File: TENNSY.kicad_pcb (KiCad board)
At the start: 2 copper layers, 120 x 160 mm, 27 parts, among them J1 HEADER_2, J2 HEADER_2, U1 Teensy4.0, U2 DRV8872, U3 QRE1113, U4 QRE1113, U5 QRE1113, U6 QRE1113, U7 QRE1113, U8 DRV8872

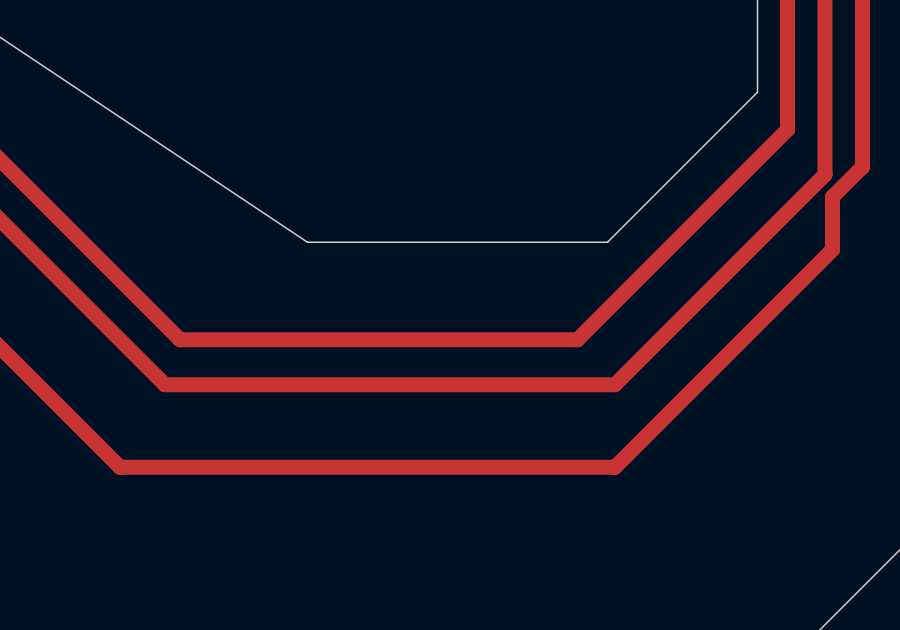
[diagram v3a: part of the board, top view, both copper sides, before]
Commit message: modificaciones
se modifico sch,pcb:
se agrego una llave
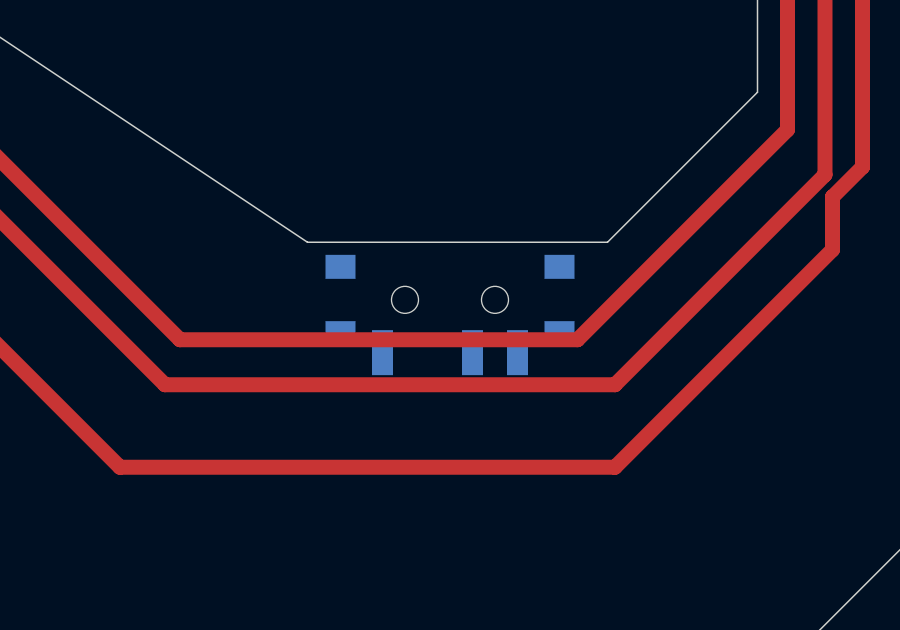
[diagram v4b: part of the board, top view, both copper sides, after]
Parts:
- added REF**: SW_SPDT_PCM12, Button_Switch_SMD:SW_SPDT_PCM12, B.Cu at (134.8, 137.2)
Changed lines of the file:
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@@
     (tracks 125)
     (zones 0)
-    (modules 27)
+    (modules 28)
     (nets 20)
   )
@@
     (add_net "Net-(R9-Pad2)")
   )
+  (module Button_Switch_SMD:SW_SPDT_PCM12 (layer B.Cu)
+    (at 134.75 137.25)
+    (descr "Ultraminiature Surface Mount Slide Switch, right-angle, https://www.ckswitches.com/media/1424/pcm.pdf")
+    (attr smd)
+    (fp_text reference REF** (at 0 3.2) (layer B.SilkS)
+      (effects (font (size 1 1) (thickness 0.15)) (justify mirror))
+    )
+    (fp_text value SW_SPDT_PCM12 (at 0 -4.25) (layer B.Fab)
+      (effects (font (size 1 1) (thickness 0.15)) (justify mirror))
+    )
+    (fp_line (start 3.45 -0.72) (end 3.45 0.07) (layer B.SilkS) (width 0.12))
+    (fp_line (start -3.45 0.07) (end -3.45 -0.72) (layer B.SilkS) (width 0.12))
+    (fp_line (start -1.6 1.12) (end 0.1 1.12) (layer B.SilkS) (width 0.12))
+    (fp_line (start -2.85 -1.73) (end 2.85 -1.73) (layer B.SilkS) (width 0.12))
+    (fp_line (start -0.1 -3.02) (end -0.1 -1.73) (layer B.SilkS) (width 0.12))
+    (fp_line (start -1.2 -3.23) (end -0.3 -3.23) (layer B.SilkS) (width 0.12))
+    (fp_line (start -1.4 -1.73) (end -1.4 -3.02) (layer B.SilkS) (width 0.12))
+    (fp_line (start -0.1 -3.02) (end -0.3 -3.23) (layer B.SilkS) (width 0.12))
+    (fp_line (start -1.4 -3.02) (end -1.2 -3.23) (layer B.SilkS) (width 0.12))
+    (fp_line (start -4.4 -2.1) (end -4.4 2.45) (layer B.CrtYd) (width 0.05))
+    (fp_line (start -1.65 -2.1) (end -4.4 -2.1) (layer B.CrtYd) (width 0.05))
+    (fp_line (start -1.65 -3.4) (end -1.65 -2.1) (layer B.CrtYd) (width 0.05))
+    (fp_line (start 1.65 -3.4) (end -1.65 -3.4) (layer B.CrtYd) (width 0.05))
+    (fp_line (start 1.65 -2.1) (end 1.65 -3.4) (layer B.CrtYd) (width 0.05))
+    (fp_line (start 4.4 -2.1) (end 1.65 -2.1) (layer B.CrtYd) (width 0.05))
+    (fp_line (start 4.4 2.45) (end 4.4 -2.1) (layer B.CrtYd) (width 0.05))
+    (fp_line (start -4.4 2.45) (end 4.4 2.45) (layer B.CrtYd) (width 0.05))
+    (fp_line (start 1.4 1.12) (end 1.6 1.12) (layer B.SilkS) (width 0.12))
+    (fp_line (start 3.35 1) (end -3.35 1) (layer B.Fab) (width 0.1))
+    (fp_line (start 3.35 -1.6) (end 3.35 1) (layer B.Fab) (width 0.1))
+    (fp_line (start -3.35 -1.6) (end 3.35 -1.6) (layer B.Fab) (width 0.1))
+    (fp_line (start -3.35 1) (end -3.35 -1.6) (layer B.Fab) (width 0.1))
+    (fp_line (start -0.1 -2.9) (end -0.1 -1.6) (layer B.Fab) (width 0.1))
+    (fp_line (start -0.15 -2.95) (end -0.1 -2.9) (layer B.Fab) (width 0.1))
+    (fp_line (start -0.35 -3.15) (end -0.15 -2.95) (layer B.Fab) (width 0.1))
+    (fp_line (start -1.2 -3.15) (end -0.35 -3.15) (layer B.Fab) (width 0.1))
+    (fp_line (start -1.4 -2.95) (end -1.2 -3.15) (layer B.Fab) (width 0.1))
+    (fp_line (start -1.4 -1.65) (end -1.4 -2.95) (layer B.Fab) (width 0.1))
+    (fp_text user %R (at 0 3.2) (layer B.Fab)
+      (effects (font (size 1 1) (thickness 0.15)) (justify mirror))
+    )
+    (pad "" smd rect (at -3.65 0.78) (size 1 0.8) (layers B.Cu B.Paste B.Mask))
+    (pad "" smd rect (at 3.65 0.78) (size 1 0.8) (layers B.Cu B.Paste B.Mask))
+    (pad "" smd rect (at 3.65 -1.43) (size 1 0.8) (layers B.Cu B.Paste B.Mask))
+    (pad "" smd rect (at -3.65 -1.43) (size 1 0.8) (layers B.Cu B.Paste B.Mask))
+    (pad 3 smd rect (at 2.25 1.43) (size 0.7 1.5) (layers B.Cu B.Paste B.Mask))
+    (pad 2 smd rect (at 0.75 1.43) (size 0.7 1.5) (layers B.Cu B.Paste B.Mask))
+    (pad 1 smd rect (at -2.25 1.43) (size 0.7 1.5) (layers B.Cu B.Paste B.Mask))
+    (pad "" np_thru_hole circle (at 1.5 -0.33) (size 0.9 0.9) (drill 0.9) (layers *.Cu *.Mask))
+    (pad "" np_thru_hole circle (at -1.5 -0.33) (size 0.9 0.9) (drill 0.9) (layers *.Cu *.Mask))
+    (model ${KISYS3DMOD}/Button_Switch_SMD.3dshapes/SW_SPDT_PCM12.wrl
+      (at (xyz 0 0 0))
+      (scale (xyz 1 1 1))
+      (rotate (xyz 0 0 0))
+    )
+  )
   (module EESTN5:Pololu_Micro_Con_Soporte_Simple (layer B.Cu)

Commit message: MODIFICACIONES
se modifico el sch y pcb
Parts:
- added C3: CAPAPOL, EESTN5:CAP_ELEC_SMD_4X5.5, F.Cu at (47.8, 144.7)
- added C4: C, EESTN5:C_1206, F.Cu at (38.0, 146.0)
- added Display1: SSD1306-SSD1306-128x64_OLED, EESTN5:128x64OLED, F.Cu at (87.5, 133.0)
- added J3: Conn_01X03, Button_Switch_SMD:SW_SPDT_PCM12, F.Cu at (49.1, 138.0)
- added J4: TB_1X2, EESTN5:BORNERA2_DUO, F.Cu at (113.8, 148.8)
- added LED1: LED, EESTN5:LED_1206, F.Cu at (59.9, 150.0)
- added LED2: LED, EESTN5:LED_1206, F.Cu at (65.2, 147.3)
- added LED3: LED, EESTN5:LED_1206, F.Cu at (58.8, 156.5)
- added LED4: LED, EESTN5:LED_1206, F.Cu at (59.2, 147.3)
- added Q1: 2N7002, EESTN5:SOT23, F.Cu at (59.0, 153.3)
- added Q2: 2N7002, EESTN5:SOT23, F.Cu at (66.0, 140.7)
- added Q3: 2N7002, EESTN5:SOT23, F.Cu at (63.1, 153.3)
- added R13: R, EESTN5:R_1206, F.Cu at (57.1, 136.8)
- added R14: R, EESTN5:R_1206, F.Cu at (44.8, 148.0)
- added R15: R, EESTN5:R_1206, F.Cu at (54.7, 143.7)
- added R16: R, EESTN5:R_1206, F.Cu at (63.2, 136.8)
- added R17: R, EESTN5:R_1206, F.Cu at (38.0, 148.5)
- added R18: R, EESTN5:R_1206, F.Cu at (53.5, 147.8)
- added R19: R, EESTN5:R_1206, F.Cu at (67.4, 150.2)
- added R20: R, EESTN5:R_1206, F.Cu at (60.8, 140.5)
- added R21: R, EESTN5:R_1206, F.Cu at (60.8, 144.1)
- added SW1: SW_DIP_x02, EESTN5:DIP-4_PC817, F.Cu at (34.5, 137.1)
- moved U8 2.00 mm to (66.0, 165.2)
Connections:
- U1 pad 33: (no net) -> /VIN

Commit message: modificaciones
se realizo modificaciones en el sch y pcb, proyecto en su 70% para su finalizacion
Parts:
- removed the REF** at (134.8, 137.2)
- added C5: C, EESTN5:C_1206, F.Cu at (69.3, 127.3)
- added U9: LM1117-SOT, EESTN5:SOT223, F.Cu at (62.8, 134.2)
- J3: footprint Button_Switch_SMD:SW_SPDT_PCM12 -> EESTN5:Pin_Strip_3
- SW1: footprint EESTN5:DIP-4_PC817 -> EESTN5:Dip_SW_2-300
- moved SW1 94.8 mm to (129.0, 144.1), turned to 270 degrees
- moved J4 69.2 mm to (45.2, 139.0), turned to 180 degrees
- moved R17 65.8 mm to (101.9, 132.6)
- moved R20 64.3 mm to (124.8, 146.8), turned to 180 degrees
- moved R21 64.0 mm to (124.8, 144.1), turned to 180 degrees
- moved J1 61.5 mm to (62.0, 181.5)
- moved R14 59.9 mm to (101.9, 129.9)
- moved R12 58.2 mm to (122.4, 175.6), turned to 270 degrees
- moved LED4 53.2 mm to (111.8, 138.9)
- moved LED1 52.3 mm to (111.8, 143.0)
- moved U8 51.8 mm to (116.5, 177.0), turned to 270 degrees
- moved R11 51.2 mm to (56.9, 178.8), turned to 90 degrees
- moved J2 49.5 mm to (118.0, 181.5)
- moved U2 48.0 mm to (63.5, 176.8), turned to 90 degrees
- moved LED2 47.0 mm to (111.8, 141.0)
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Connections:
- Display1 pad 3: (no net) -> /SCL
- Display1 pad 4: (no net) -> /SDA
- U1 pad 10: (no net) -> /MODO2
- U1 pad 11: (no net) -> /MODO3
- U1 pad 25: (no net) -> /SDA
- U1 pad 26: (no net) -> /SCL
- U1 pad 33: /VIN -> VCC
- U1 pad 4: (no net) -> /M1A
- U1 pad 5: (no net) -> /M1B
- U1 pad 7: (no net) -> /M2A
- U1 pad 8: (no net) -> /M2B
- U1 pad 9: (no net) -> /MODE1
- U2 pad 2: (no net) -> /M1B
- U2 pad 3: (no net) -> /M1A
- U8 pad 2: (no net) -> /M2B
- U8 pad 3: (no net) -> /M2A
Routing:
- net /VIN: track 0.00 -> 78.3 mm, vias 0 -> 4
- net /A3: track 226.9 -> 157.9 mm
- net VCC: track 0.00 -> 62.0 mm
- net /A6: track 213.5 -> 153.0 mm
- net /M2A: track 0.00 -> 50.5 mm
- net /M2B: track 0.00 -> 46.4 mm
- net /M1B: track 0.00 -> 43.4 mm
- net /M1A: track 0.00 -> 40.6 mm
- net Net-(C3-Pad1): track 0.00 -> 28.4 mm
- net Net-(Q1-Pad2): track 0.00 -> 20.9 mm
- net Net-(J3-Pad2): track 0.00 -> 16.6 mm
- net Net-(Q2-Pad2): track 0.00 -> 14.1 mm
- net Net-(LED4-Pad1): track 0.00 -> 13.6 mm
- net Net-(LED2-Pad1): track 0.00 -> 13.5 mm
- net Net-(Q3-Pad2): track 0.00 -> 11.2 mm
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
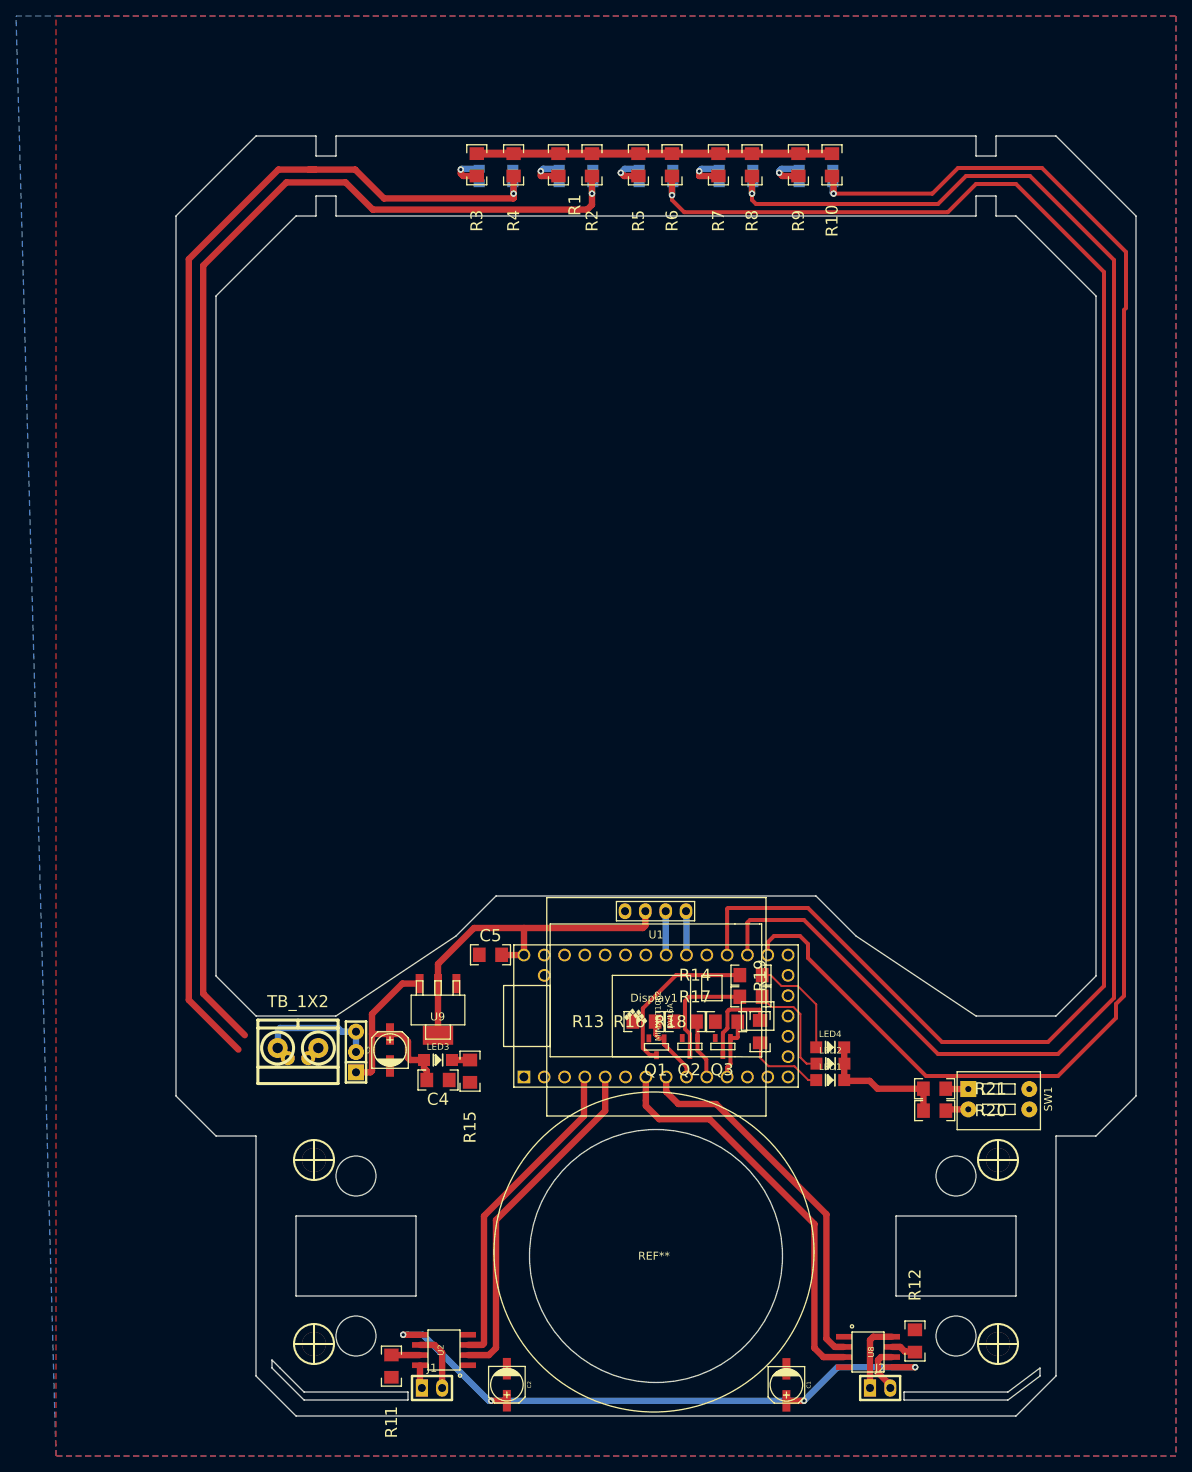
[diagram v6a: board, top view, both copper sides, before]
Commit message: modificaciones
se termino pcb,se agregaron: buzzer,imagen de sch de un modulo gitoscopio
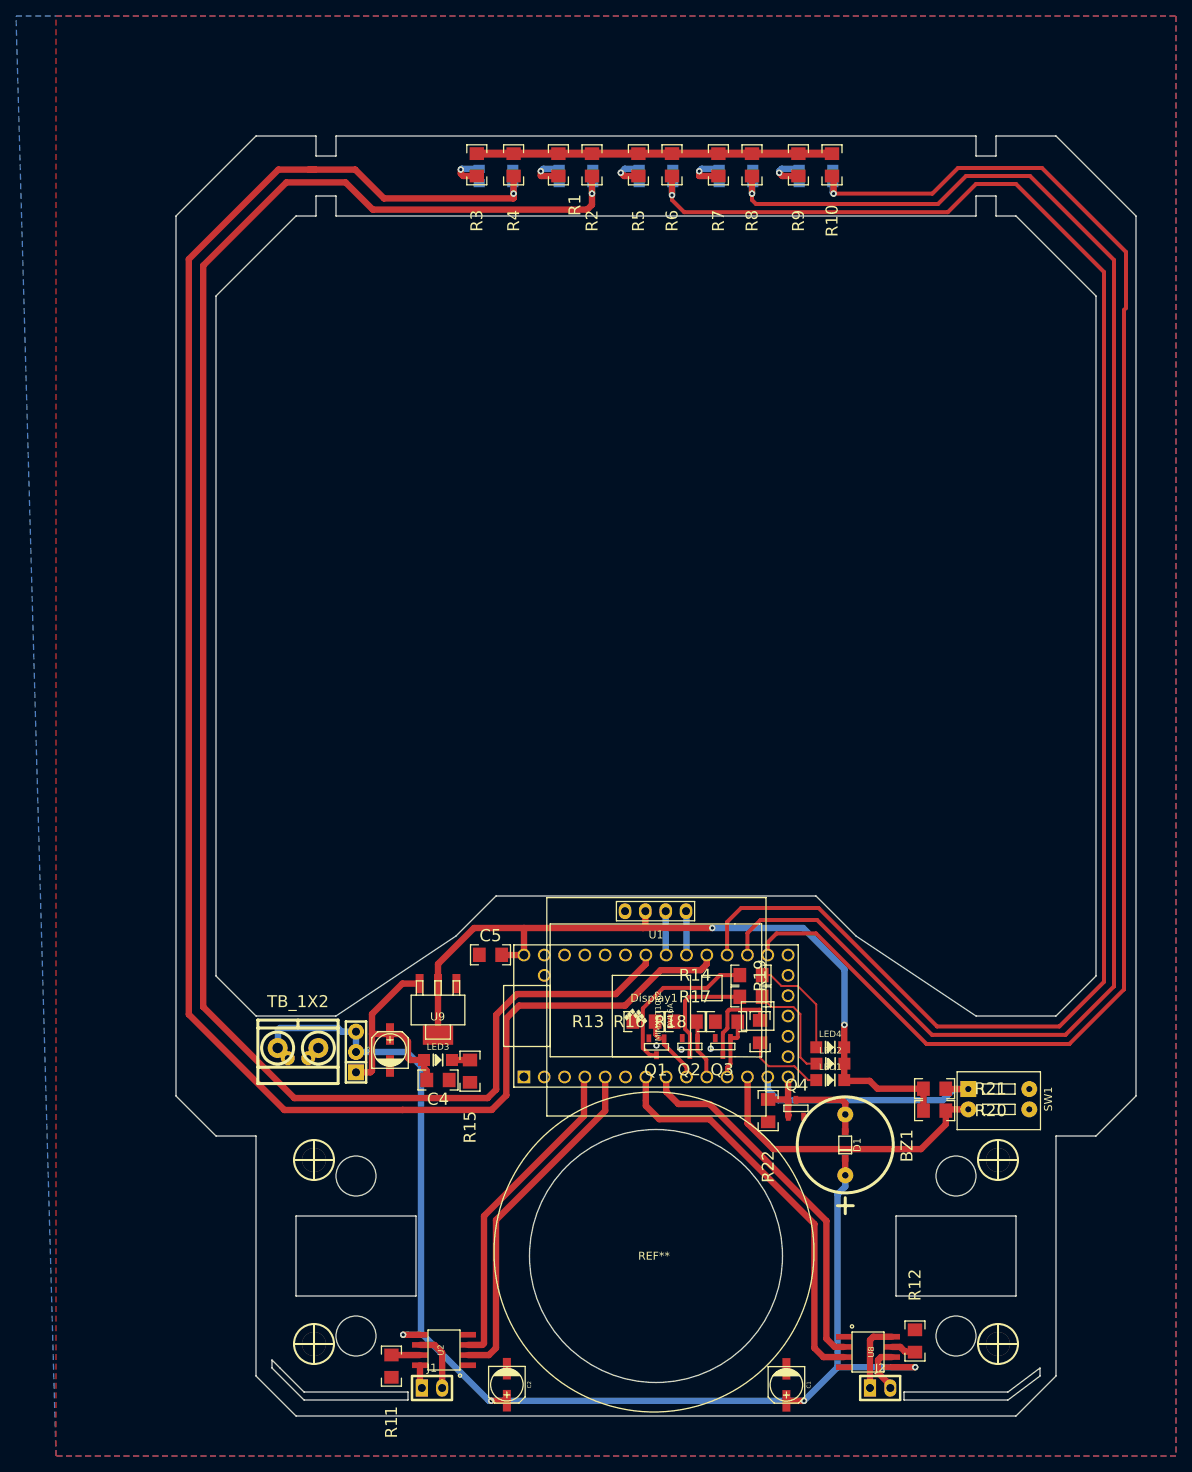
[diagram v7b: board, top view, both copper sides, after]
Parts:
- added BZ1: Buzzer, EESTN5:Buzzer_12mm, F.Cu at (113.7, 151.1)
- added D1: DIODE, EESTN5:sod123, F.Cu at (113.7, 151.1)
- added Q4: 2N7002, EESTN5:SOT23, F.Cu at (107.5, 146.5)
- added R22: R, EESTN5:R_1206, F.Cu at (104.0, 146.8)
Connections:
- J3 pad 2: Net-(J3-Pad2) -> /VIN
- J3 pad 3: Net-(J3-Pad2) -> /VIN
- J4 pad 2: Net-(J3-Pad2) -> /VIN
- R2 pad 2: /A3 -> /A6
- R4 pad 2: /A6 -> /A3
- U1 pad 12: (no net) -> /ESTRATEGIAS1
- U1 pad 13: (no net) -> /ESTRATEGIAS2
- U1 pad 14: (no net) -> /buzzer
- U3 pad 3: /A3 -> /A6
- U4 pad 3: /A6 -> /A3
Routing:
- net /VIN: track 78.3 -> 164.0 mm
- net /A6: track 153.0 -> 225.8 mm
- net /A3: track 157.9 -> 230.1 mm
- net VCC: track 62.0 -> 99.1 mm, vias 0 -> 2
- net /ESTRATEGIAS1: track 2.88 -> 37.8 mm
- net /ESTRATEGIAS2: track 2.84 -> 30.6 mm
- net Net-(J3-Pad2): track 16.6 -> 0.00 mm
- net Net-(BZ1-Pad2): track 0.00 -> 9.88 mm
- net /buzzer: track 0.00 -> 8.24 mm
- net /A0: track 198.8 -> 193.3 mm
- net /A1: track 207.7 -> 204.1 mm
- net /A2: track 217.2 -> 214.3 mm
- net GND: vias 0 -> 3
